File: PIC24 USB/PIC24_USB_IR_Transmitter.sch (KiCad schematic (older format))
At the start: 25 parts, among them CON1 USB-MINI-B, P1 CONN_6, P2 CONN_4, P3 CONN_4, P4 CONN_8, P5 CONN_4, P6 CONN_1, P7 CONN_8, P8 CONN_8X2, Q1 2N7002, U2 LM1117_SOT223_3V3, U4 MCP48X2

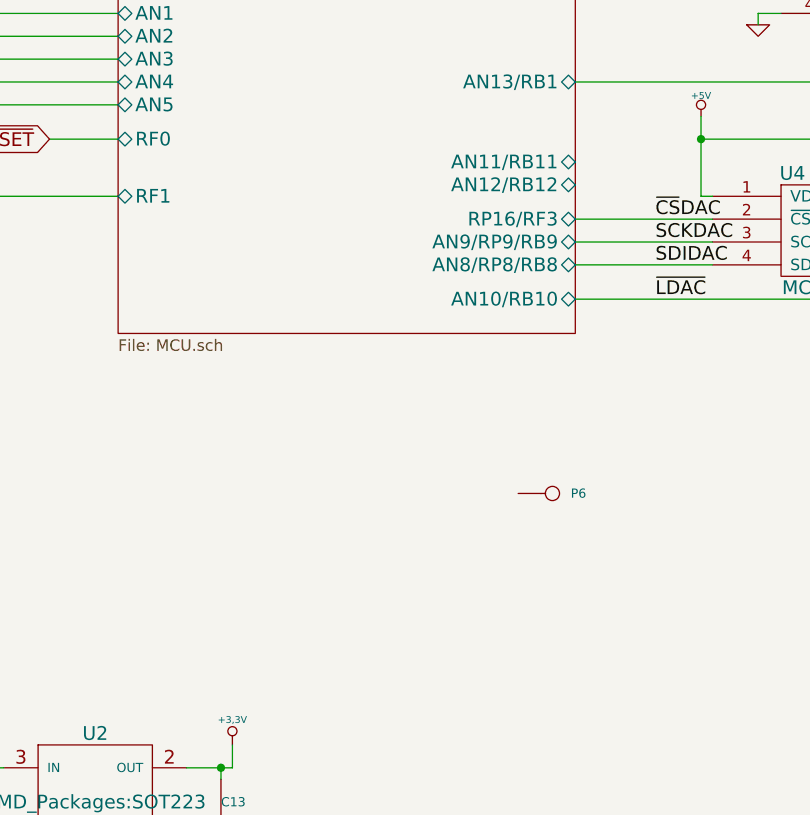
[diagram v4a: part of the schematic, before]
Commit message: shrinked, added temp sensor, updated gerbers and submitted them
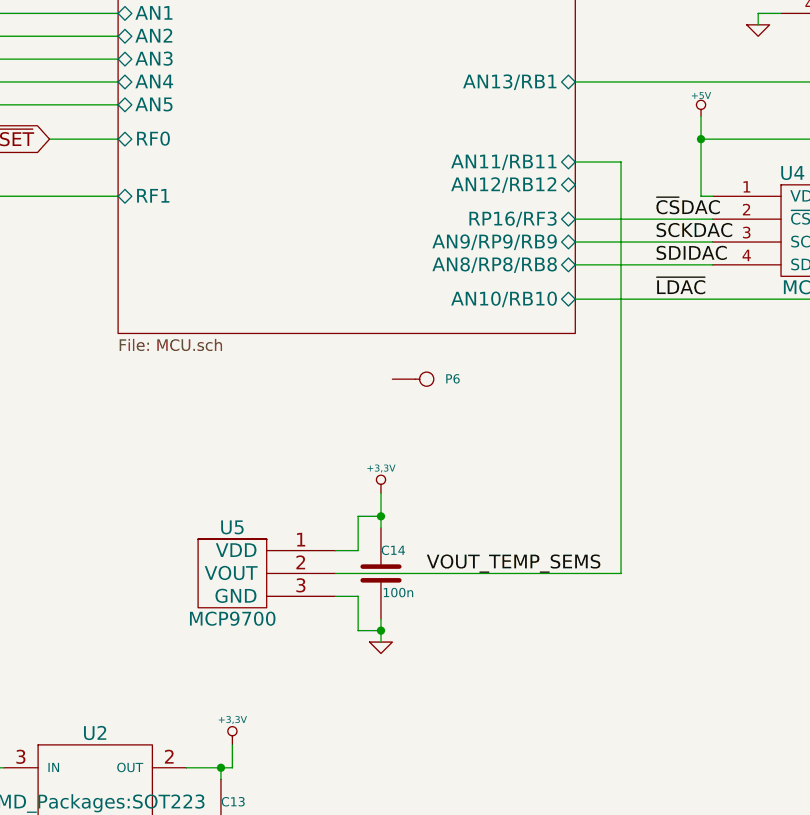
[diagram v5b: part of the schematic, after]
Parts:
- added C14: 100n, SMD_Packages:SMD-0603_c, symbol C
- added U5: MCP9700, symbol MCP9700
- P6: footprint Symbols:Symbol_OSHW-Logo_CopperTop -> Symbols:Symbol_OSHW-Logo_SilkScreen
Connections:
- net +3.3V: now also C14.1, U5.1 (VDD)
- net GND: now also C14.2, U5.3 (GND)
- new net VOUT_TEMP_SEMS: U5.2 (VOUT)
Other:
- moved on the sheet: P6
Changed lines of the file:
@@
 ~MCLR~
 $Comp
-L GND #PWR34
+L GND #PWR36
 U 1 1 52D45877
 P 10800 4000
-F 0 "#PWR34" H 10800 4000 30  0001 C CNN
+F 0 "#PWR36" H 10800 4000 30  0001 C CNN
 F 1 "GND" H 10800 3930 30  0001 C CNN
 F 2 "" H 10800 4000 60  0000 C CNN
@@
 $EndComp
 $Comp
-L +5V #PWR33
+L +5V #PWR35
 U 1 1 52D45886
 P 10800 2450
-F 0 "#PWR33" H 10800 2540 20  0001 C CNN
+F 0 "#PWR35" H 10800 2540 20  0001 C CNN
 F 1 "+5V" H 10800 2540 30  0000 C CNN
 F 2 "" H 10800 2450 60  0000 C CNN
@@
 $EndComp
 $Comp
-L GND #PWR28
+L GND #PWR30
 U 1 1 52D4649C
 P 8350 3450
-F 0 "#PWR28" H 8350 3450 30  0001 C CNN
+F 0 "#PWR30" H 8350 3450 30  0001 C CNN
 F 1 "GND" H 8350 3380 30  0001 C CNN
 F 2 "" H 8350 3450 60  0000 C CNN
@@
 	7550 2650 9200 2650
 $Comp
-L +3,3V #PWR27
+L +3,3V #PWR29
 U 1 1 53EA7361
 P 8350 3050
-F 0 "#PWR27" H 8350 3010 30  0001 C CNN
+F 0 "#PWR29" H 8350 3010 30  0001 C CNN
 F 1 "+3,3V" H 8350 3160 30  0000 C CNN
 F 2 "" H 8350 3050 60  0000 C CNN
@@
 	9550 3950 9550 4750
 $Comp
-L GND #PWR30
+L GND #PWR32
 U 1 1 53EB3792
 P 9550 4750
-F 0 "#PWR30" H 9550 4750 30  0001 C CNN
+F 0 "#PWR32" H 9550 4750 30  0001 C CNN
 F 1 "GND" H 9550 4680 30  0001 C CNN
 F 2 "" H 9550 4750 60  0000 C CNN
@@
 Connection ~ 8100 3950
 $Comp
-L GND #PWR32
+L GND #PWR34
 U 1 1 53EB8094
 P 9800 4600
-F 0 "#PWR32" H 9800 4600 30  0001 C CNN
+F 0 "#PWR34" H 9800 4600 30  0001 C CNN
 F 1 "GND" H 9800 4530 30  0001 C CNN
 F 2 "" H 9800 4600 60  0000 C CNN
@@
 VOUTB
 $Comp
-L GND #PWR29
+L GND #PWR31
 U 1 1 53EB8CF7
 P 9350 5300
-F 0 "#PWR29" H 9350 5300 30  0001 C CNN
+F 0 "#PWR31" H 9350 5300 30  0001 C CNN
 F 1 "GND" H 9350 5230 30  0001 C CNN
 F 2 "" H 9350 5300 60  0000 C CNN
@@
 ~LDAC~
 $Comp
-L +5V #PWR26
+L +5V #PWR28
 U 1 1 53EC555A
 P 8100 3850
-F 0 "#PWR26" H 8100 3940 20  0001 C CNN
+F 0 "#PWR28" H 8100 3940 20  0001 C CNN
 F 1 "+5V" H 8100 3940 30  0000 C CNN
 F 2 "" H 8100 3850 60  0000 C CNN
@@
 $EndComp
 $Comp
-L +5V #PWR31
+L +5V #PWR33
 U 1 1 53EC5C84
 P 9800 4100
-F 0 "#PWR31" H 9800 4190 20  0001 C CNN
+F 0 "#PWR33" H 9800 4190 20  0001 C CNN
 F 1 "+5V" H 9800 4190 30  0000 C CNN
 F 2 "" H 9800 4100 60  0000 C CNN
@@
 L CONN_1 P6
 U 1 1 53EB4765
-P 7450 5500
-F 0 "P6" H 7530 5500 40  0000 L CNN
-F 1 "CONN_1" H 7450 5555 30  0001 C CNN
-F 2 "Symbols:Symbol_OSHW-Logo_CopperTop" H 7450 5500 60  0001 C CNN
-F 3 "" H 7450 5500 60  0000 C CNN
-	1    7450 5500
+P 6900 5000
+F 0 "P6" H 6980 5000 40  0000 L CNN
+F 1 "CONN_1" H 6900 5055 30  0001 C CNN
+F 2 "Symbols:Symbol_OSHW-Logo_SilkScreen" H 6900 5000 60  0001 C CNN
+F 3 "" H 6900 5000 60  0000 C CNN
+	1    6900 5000
 	1    0    0    -1
 $EndComp
@@
 	-1   0    0    -1
 $EndComp
+$Comp
+L MCP9700 U5
+U 1 1 53EC8FC0
+P 6100 5900
+F 0 "U5" H 6050 6150 60  0000 C CNN
+F 1 "MCP9700" H 6050 5750 60  0000 C CNN
+F 2 "" H 6150 5900 60  0000 C CNN
+F 3 "" H 6150 5900 60  0000 C CNN
+	1    6100 5900
+	1    0    0    -1
+$EndComp
+Wire Wire Line
+	7550 4050 7750 4050
+Wire Wire Line
+	7750 4050 7750 5850
+Wire Wire Line
+	7750 5850 6500 5850
+Text Label 6900 5850 0    60   ~ 0
+VOUT_TEMP_SEMS
+$Comp
+L GND #PWR27
+U 1 1 53ECDE47
+P 6700 6150
+F 0 "#PWR27" H 6700 6150 30  0001 C CNN
+F 1 "GND" H 6700 6080 30  0001 C CNN
+F 2 "" H 6700 6150 60  0000 C CNN
+F 3 "" H 6700 6150 60  0000 C CNN
+	1    6700 6150
+	1    0    0    -1
+$EndComp
+$Comp
+L C C14
+U 1 1 53ECF8B3
+P 6700 5850
+F 0 "C14" H 6700 5950 40  0000 L CNN
+F 1 "100n" H 6706 5765 40  0000 L CNN
+F 2 "SMD_Packages:SMD-0603_c" H 6738 5700 30  0001 C CNN
+F 3 "" H 6700 5850 60  0000 C CNN
+	1    6700 5850
+	1    0    0    -1
+$EndComp
+$Comp
+L +3,3V #PWR26
+U 1 1 53ED014E
+P 6700 5500
+F 0 "#PWR26" H 6700 5460 30  0001 C CNN
+F 1 "+3,3V" H 6700 5610 30  0000 C CNN
+F 2 "" H 6700 5500 60  0000 C CNN
+F 3 "" H 6700 5500 60  0000 C CNN
+	1    6700 5500
+	1    0    0    -1
+$EndComp
+Wire Wire Line
+	6500 5750 6600 5750
+Wire Wire Line
+	6600 5750 6600 5600
+Wire Wire Line
+	6600 5600 6700 5600
+Wire Wire Line
+	6700 5500 6700 5650
+Connection ~ 6700 5600
+Wire Wire Line
+	6500 5950 6600 5950
+Wire Wire Line
+	6600 5950 6600 6100
+Wire Wire Line
+	6600 6100 6700 6100
+Wire Wire Line
+	6700 6050 6700 6150
+Connection ~ 6700 6100
 $EndSCHEMATC

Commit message: nightly commit with canges in the schematic
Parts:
- U5: footprint (none) -> Discret:TO92-123
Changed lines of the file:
@@
 F 0 "U5" H 6050 6150 60  0000 C CNN
 F 1 "MCP9700" H 6050 5750 60  0000 C CNN
-F 2 "" H 6150 5900 60  0000 C CNN
+F 2 "Discret:TO92-123" H 6150 5900 60  0001 C CNN
 F 3 "" H 6150 5900 60  0000 C CNN
 	1    6100 5900

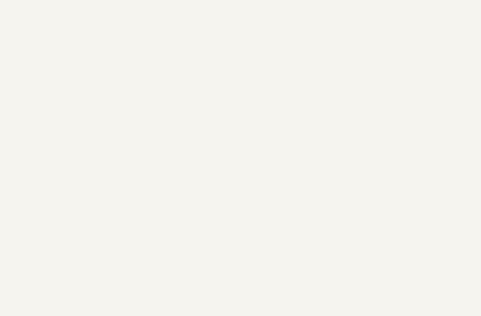
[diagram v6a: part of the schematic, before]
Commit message: changed wrong polarity of led matrix in schematic, started correcting the layout
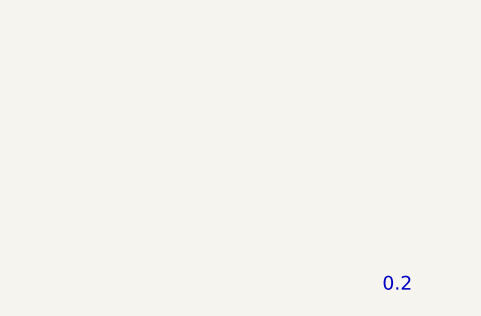
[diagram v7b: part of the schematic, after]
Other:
- note added: "0.2"
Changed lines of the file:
@@
 Connection ~ 950  3150
 $Comp
-L GND #PWR9
+L GND #PWR01
 U 1 1 52D43B6B
 P 2200 3350
-F 0 "#PWR9" H 2200 3350 30  0001 C CNN
+F 0 "#PWR01" H 2200 3350 30  0001 C CNN
 F 1 "GND" H 2200 3280 30  0001 C CNN
 F 2 "" H 2200 3350 60  0000 C CNN
@@
 	2250 2000 2250 1950
 $Comp
-L +5V #PWR10
+L +5V #PWR02
 U 1 1 52D43B8D
 P 2250 1950
-F 0 "#PWR10" H 2250 2040 20  0001 C CNN
+F 0 "#PWR02" H 2250 2040 20  0001 C CNN
 F 1 "+5V" H 2250 2040 30  0000 C CNN
 F 2 "" H 2250 1950 60  0000 C CNN
@@
 $EndComp
 $Comp
-L +5V #PWR2
+L +5V #PWR03
 U 1 1 52D43BD6
 P 1200 1050
-F 0 "#PWR2" H 1200 1140 20  0001 C CNN
+F 0 "#PWR03" H 1200 1140 20  0001 C CNN
 F 1 "+5V" H 1200 1140 30  0000 C CNN
 F 2 "" H 1200 1050 60  0000 C CNN
@@
 $EndComp
 $Comp
-L GND #PWR3
+L GND #PWR04
 U 1 1 52D43BDC
 P 1200 1650
-F 0 "#PWR3" H 1200 1650 30  0001 C CNN
+F 0 "#PWR04" H 1200 1650 30  0001 C CNN
 F 1 "GND" H 1200 1580 30  0001 C CNN
 F 2 "" H 1200 1650 60  0000 C CNN
@@
 	2450 5650 2450 5900
 $Comp
-L GND #PWR11
+L GND #PWR05
 U 1 1 52D450A4
 P 2450 5900
-F 0 "#PWR11" H 2450 5900 30  0001 C CNN
+F 0 "#PWR05" H 2450 5900 30  0001 C CNN
 F 1 "GND" H 2450 5830 30  0001 C CNN
 F 2 "" H 2450 5900 60  0000 C CNN
@@
 ~MCLR~
 $Comp
-L GND #PWR36
+L GND #PWR06
 U 1 1 52D45877
 P 10800 4000
-F 0 "#PWR36" H 10800 4000 30  0001 C CNN
+F 0 "#PWR06" H 10800 4000 30  0001 C CNN
 F 1 "GND" H 10800 3930 30  0001 C CNN
 F 2 "" H 10800 4000 60  0000 C CNN
@@
 $EndComp
 $Comp
-L +5V #PWR35
+L +5V #PWR07
 U 1 1 52D45886
 P 10800 2450
-F 0 "#PWR35" H 10800 2540 20  0001 C CNN
+F 0 "#PWR07" H 10800 2540 20  0001 C CNN
 F 1 "+5V" H 10800 2540 30  0000 C CNN
 F 2 "" H 10800 2450 60  0000 C CNN
@@
 	1650 850  1650 950
 $Comp
-L GND #PWR5
+L GND #PWR08
 U 1 1 52D45EC1
 P 1650 1950
-F 0 "#PWR5" H 1650 1950 30  0001 C CNN
+F 0 "#PWR08" H 1650 1950 30  0001 C CNN
 F 1 "GND" H 1650 1880 30  0001 C CNN
 F 2 "" H 1650 1950 60  0000 C CNN
@@
 $EndComp
 $Comp
-L +5V #PWR4
+L +5V #PWR09
 U 1 1 52D45EC7
 P 1650 850
-F 0 "#PWR4" H 1650 940 20  0001 C CNN
+F 0 "#PWR09" H 1650 940 20  0001 C CNN
 F 1 "+5V" H 1650 940 30  0000 C CNN
 F 2 "" H 1650 850 60  0000 C CNN
@@
 $EndComp
 $Comp
-L GND #PWR30
+L GND #PWR010
 U 1 1 52D4649C
 P 8350 3450
-F 0 "#PWR30" H 8350 3450 30  0001 C CNN
+F 0 "#PWR010" H 8350 3450 30  0001 C CNN
 F 1 "GND" H 8350 3380 30  0001 C CNN
 F 2 "" H 8350 3450 60  0000 C CNN
@@
 $EndComp
 $Comp
-L GND #PWR16
+L GND #PWR011
 U 1 1 52D464B4
 P 3700 5050
-F 0 "#PWR16" H 3700 5050 30  0001 C CNN
+F 0 "#PWR011" H 3700 5050 30  0001 C CNN
 F 1 "GND" H 3700 4980 30  0001 C CNN
 F 2 "" H 3700 5050 60  0000 C CNN
@@
 $EndComp
 $Comp
-L +5V #PWR15
+L +5V #PWR012
 U 1 1 52D464BA
 P 3700 4650
-F 0 "#PWR15" H 3700 4740 20  0001 C CNN
+F 0 "#PWR012" H 3700 4740 20  0001 C CNN
 F 1 "+5V" H 3700 4740 30  0000 C CNN
 F 2 "" H 3700 4650 60  0000 C CNN
@@
 ICSP
 $Comp
-L +5V #PWR17
+L +5V #PWR013
 U 1 1 52D469A9
 P 3800 4200
-F 0 "#PWR17" H 3800 4290 20  0001 C CNN
+F 0 "#PWR013" H 3800 4290 20  0001 C CNN
 F 1 "+5V" H 3800 4290 30  0000 C CNN
 F 2 "" H 3800 4200 60  0000 C CNN
@@
 $EndComp
 $Comp
-L +5V #PWR18
+L +5V #PWR014
 U 1 1 52D469AF
 P 3950 4200
-F 0 "#PWR18" H 3950 4290 20  0001 C CNN
+F 0 "#PWR014" H 3950 4290 20  0001 C CNN
 F 1 "+5V" H 3950 4290 30  0000 C CNN
 F 2 "" H 3950 4200 60  0000 C CNN
@@
 $EndComp
 $Comp
-L GND #PWR8
+L GND #PWR015
 U 1 1 52D8FECF
 P 2000 7250
-F 0 "#PWR8" H 2000 7250 30  0001 C CNN
+F 0 "#PWR015" H 2000 7250 30  0001 C CNN
 F 1 "GND" H 2000 7180 30  0001 C CNN
 F 2 "" H 2000 7250 60  0000 C CNN
@@
 	2000 6900 2000 7250
 $Comp
-L +5V #PWR7
+L +5V #PWR016
 U 1 1 52D8FF66
 P 2000 6350
-F 0 "#PWR7" H 2000 6440 20  0001 C CNN
+F 0 "#PWR016" H 2000 6440 20  0001 C CNN
 F 1 "+5V" H 2000 6440 30  0000 C CNN
 F 2 "" H 2000 6350 60  0000 C CNN
@@
 $EndComp
 $Comp
-L +5V #PWR22
+L +5V #PWR017
 U 1 1 53DC073B
 P 4950 6550
-F 0 "#PWR22" H 4950 6640 20  0001 C CNN
+F 0 "#PWR017" H 4950 6640 20  0001 C CNN
 F 1 "+5V" H 4950 6640 30  0000 C CNN
 F 2 "" H 4950 6550 60  0000 C CNN
@@
 	6050 6700 6050 6600
 $Comp
-L +3,3V #PWR25
+L +3,3V #PWR018
 U 1 1 53DC0908
 P 6050 6600
-F 0 "#PWR25" H 6050 6560 30  0001 C CNN
+F 0 "#PWR018" H 6050 6560 30  0001 C CNN
 F 1 "+3,3V" H 6050 6710 30  0000 C CNN
 F 2 "" H 6050 6600 60  0000 C CNN
@@
 $EndComp
 $Comp
-L GND #PWR23
+L GND #PWR019
 U 1 1 53DC0948
 P 5450 7300
-F 0 "#PWR23" H 5450 7300 30  0001 C CNN
+F 0 "#PWR019" H 5450 7300 30  0001 C CNN
 F 1 "GND" H 5450 7230 30  0001 C CNN
 F 2 "" H 5450 7300 60  0000 C CNN
@@
 	5450 7200 5450 7300
 $Comp
-L GND #PWR24
+L GND #PWR020
 U 1 1 53DC0A13
 P 6000 7300
-F 0 "#PWR24" H 6000 7300 30  0001 C CNN
+F 0 "#PWR020" H 6000 7300 30  0001 C CNN
 F 1 "GND" H 6000 7230 30  0001 C CNN
 F 2 "" H 6000 7300 60  0000 C CNN
@@
 	4750 2150 5550 2150
 $Comp
-L +3,3V #PWR6
+L +3,3V #PWR021
 U 1 1 53DEBDEC
 P 1900 4850
-F 0 "#PWR6" H 1900 4810 30  0001 C CNN
+F 0 "#PWR021" H 1900 4810 30  0001 C CNN
 F 1 "+3,3V" H 1900 4960 30  0000 C CNN
 F 2 "" H 1900 4850 60  0000 C CNN
@@
 	7550 2650 9200 2650
 $Comp
-L +3,3V #PWR29
+L +3,3V #PWR022
 U 1 1 53EA7361
 P 8350 3050
-F 0 "#PWR29" H 8350 3010 30  0001 C CNN
+F 0 "#PWR022" H 8350 3010 30  0001 C CNN
 F 1 "+3,3V" H 8350 3160 30  0000 C CNN
 F 2 "" H 8350 3050 60  0000 C CNN
@@
 $EndComp
 $Comp
-L +3,3V #PWR19
+L +3,3V #PWR023
 U 1 1 53EA6763
 P 4400 3150
-F 0 "#PWR19" H 4400 3110 30  0001 C CNN
+F 0 "#PWR023" H 4400 3110 30  0001 C CNN
 F 1 "+3,3V" H 4400 3260 30  0000 C CNN
 F 2 "" H 4400 3150 60  0000 C CNN
@@
 $EndComp
 $Comp
-L GND #PWR20
+L GND #PWR024
 U 1 1 53EA6786
 P 4400 4000
-F 0 "#PWR20" H 4400 4000 30  0001 C CNN
+F 0 "#PWR024" H 4400 4000 30  0001 C CNN
 F 1 "GND" H 4400 3930 30  0001 C CNN
 F 2 "" H 4400 4000 60  0000 C CNN
@@
 	3100 850  3100 1700
 $Comp
-L GND #PWR13
+L GND #PWR025
 U 1 1 53EA8972
 P 3450 2000
-F 0 "#PWR13" H 3450 2000 30  0001 C CNN
+F 0 "#PWR025" H 3450 2000 30  0001 C CNN
 F 1 "GND" H 3450 1930 30  0001 C CNN
 F 2 "" H 3450 2000 60  0000 C CNN
@@
 	3250 1400 3550 1400
 $Comp
-L +5V #PWR14
+L +5V #PWR026
 U 1 1 53EAABDE
 P 3500 1150
-F 0 "#PWR14" H 3500 1240 20  0001 C CNN
+F 0 "#PWR026" H 3500 1240 20  0001 C CNN
 F 1 "+5V" H 3500 1240 30  0000 C CNN
 F 2 "" H 3500 1150 60  0000 C CNN
@@
 $EndComp
 $Comp
-L +3,3V #PWR12
+L +3,3V #PWR027
 U 1 1 53EAAC01
 P 3350 1150
-F 0 "#PWR12" H 3350 1110 30  0001 C CNN
+F 0 "#PWR027" H 3350 1110 30  0001 C CNN
 F 1 "+3,3V" H 3350 1260 30  0000 C CNN
 F 2 "" H 3350 1150 60  0000 C CNN
@@
 	9550 3950 9550 4750
 $Comp
-L GND #PWR32
+L GND #PWR028
 U 1 1 53EB3792
 P 9550 4750
-F 0 "#PWR32" H 9550 4750 30  0001 C CNN
+F 0 "#PWR028" H 9550 4750 30  0001 C CNN
 F 1 "GND" H 9550 4680 30  0001 C CNN
 F 2 "" H 9550 4750 60  0000 C CNN
@@
 Connection ~ 8100 3950
 $Comp
-L GND #PWR34
+L GND #PWR029
 U 1 1 53EB8094
 P 9800 4600
-F 0 "#PWR34" H 9800 4600 30  0001 C CNN
+F 0 "#PWR029" H 9800 4600 30  0001 C CNN
 F 1 "GND" H 9800 4530 30  0001 C CNN
 F 2 "" H 9800 4600 60  0000 C CNN
@@
 VOUTB
 $Comp
-L GND #PWR31
+L GND #PWR030
 U 1 1 53EB8CF7
 P 9350 5300
-F 0 "#PWR31" H 9350 5300 30  0001 C CNN
+F 0 "#PWR030" H 9350 5300 30  0001 C CNN
 F 1 "GND" H 9350 5230 30  0001 C CNN
 F 2 "" H 9350 5300 60  0000 C CNN
@@
 ~LDAC~
 $Comp
-L +5V #PWR28
+L +5V #PWR031
 U 1 1 53EC555A
 P 8100 3850
-F 0 "#PWR28" H 8100 3940 20  0001 C CNN
+F 0 "#PWR031" H 8100 3940 20  0001 C CNN
 F 1 "+5V" H 8100 3940 30  0000 C CNN
 F 2 "" H 8100 3850 60  0000 C CNN
@@
 $EndComp
 $Comp
-L +5V #PWR33
+L +5V #PWR032
 U 1 1 53EC5C84
 P 9800 4100
-F 0 "#PWR33" H 9800 4190 20  0001 C CNN
+F 0 "#PWR032" H 9800 4190 20  0001 C CNN
 F 1 "+5V" H 9800 4190 30  0000 C CNN
 F 2 "" H 9800 4100 60  0000 C CNN
@@
 replace with polyfuse\nor ferrite if needed
 $Comp
-L GND #PWR21
+L GND #PWR033
 U 1 1 53EFE3A1
 P 4450 6200
-F 0 "#PWR21" H 4450 6200 30  0001 C CNN
+F 0 "#PWR033" H 4450 6200 30  0001 C CNN
 F 1 "GND" H 4450 6130 30  0001 C CNN
 F 2 "" H 4450 6200 60  0000 C CNN
@@
 VOUTA
 $Comp
-L GND #PWR1
+L GND #PWR034
 U 1 1 52D43B2E
 P 950 3350
-F 0 "#PWR1" H 950 3350 30  0001 C CNN
+F 0 "#PWR034" H 950 3350 30  0001 C CNN
 F 1 "GND" H 950 3280 30  0001 C CNN
 F 2 "" H 950 3350 60  0000 C CNN
@@
 VOUT_TEMP_SEMS
 $Comp
-L GND #PWR27
+L GND #PWR035
 U 1 1 53ECDE47
 P 6700 6150
-F 0 "#PWR27" H 6700 6150 30  0001 C CNN
+F 0 "#PWR035" H 6700 6150 30  0001 C CNN
 F 1 "GND" H 6700 6080 30  0001 C CNN
 F 2 "" H 6700 6150 60  0000 C CNN
@@
 $EndComp
 $Comp
-L +3,3V #PWR26
+L +3,3V #PWR036
 U 1 1 53ED014E
 P 6700 5500
-F 0 "#PWR26" H 6700 5460 30  0001 C CNN
+F 0 "#PWR036" H 6700 5460 30  0001 C CNN
 F 1 "+3,3V" H 6700 5610 30  0000 C CNN
 F 2 "" H 6700 5500 60  0000 C CNN
@@
 	6700 6050 6700 6150
 Connection ~ 6700 6100
+Text Notes 10600 7650 0    60   ~ 0
+0.2
 $EndSCHEMATC
